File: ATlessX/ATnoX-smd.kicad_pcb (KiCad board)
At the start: 4 copper layers, 80 x 47 mm, 32 parts, among them J1 EXT_PWR_SW, J2 ATX, J3 AT, J4 PWR_LED, SW1 Power, U1 74LS74, U2 74LS14, U3 L7905

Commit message: Rev 3
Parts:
- added C5: 100nF, Capacitor_SMD:C_1206_3216Metric_Pad1.42x1.75mm_HandSolder, B.Cu at (111.8, 90.2)
- added C6: 100nF, Capacitor_SMD:C_1206_3216Metric_Pad1.42x1.75mm_HandSolder, B.Cu at (128.3, 91.4)
- added C7: 6.8pF, Capacitor_SMD:C_1206_3216Metric_Pad1.42x1.75mm_HandSolder, B.Cu at (119.4, 111.8)
- added C8: 6.8pF, Capacitor_SMD:C_1206_3216Metric_Pad1.42x1.75mm_HandSolder, B.Cu at (125.7, 111.8)
- added R10: 100K, Resistor_SMD:R_1206_3216Metric_Pad1.42x1.75mm_HandSolder, B.Cu at (111.8, 109.2)
- added R11: 10M, Resistor_SMD:R_1206_3216Metric_Pad1.42x1.75mm_HandSolder, B.Cu at (106.7, 101.6)
- added U4: 74HCT4060, Package_SO:SOIC-16_3.9x9.9mm_P1.27mm, B.Cu at (114.3, 99.1)
- added U5: 74HC73, Package_SO:SOIC-14_3.9x8.7mm_P1.27mm, B.Cu at (125.7, 99.1)
- added Y1: 3.2768, Crystal:Crystal_SMD_HC49-SD, B.Cu at (121.9, 108.0)
- moved C4 2.54 mm to (106.7, 95.2)
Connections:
- J2 pad 1: Net-(J2-Pad1) -> (no net)
- J2 pad 11: Net-(J2-Pad11) -> (no net)
- J2 pad 18: Net-(J2-Pad18) -> (no net)
- J2 pad 2: Net-(J2-Pad2) -> (no net)
- J3 pad 6: Net-(J3-Pad6) -> /TICK
- U1 pad 8: Net-(U1-Pad8) -> (no net)
- U1 pad 9: Net-(U1-Pad9) -> (no net)
- U2 pad 10: Net-(U2-Pad10) -> (no net)
- U2 pad 12: Net-(U2-Pad12) -> (no net)
- U2 pad 8: Net-(U2-Pad8) -> (no net)
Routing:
- net VCC: track 104.0 -> 206.7 mm, vias 1 -> 2
- net Net-(C8-Pad1): track 0.00 -> 62.5 mm
- net Net-(R10-Pad1): track 0.00 -> 18.5 mm
- net Net-(U4-Pad7): track 0.00 -> 17.9 mm, vias 0 -> 2
- net Net-(U5-Pad12): track 0.00 -> 17.7 mm, vias 0 -> 2
- net /TICK: track 0.00 -> 17.5 mm
- net Net-(C7-Pad1): track 0.00 -> 10.5 mm
- net /~PS_ON: track 68.5 -> 58.9 mm, vias 0 -> 1
- net Net-(U1-Pad4): track 28.6 -> 34.2 mm
- net Net-(C1-Pad1): track 24.0 -> 28.5 mm
- net /-12V: track 81.7 -> 85.3 mm, vias 1 -> 3
- net GND: track 412.3 -> 414.7 mm, vias 2 -> 4
- net Net-(C2-Pad1): track 22.0 -> 24.3 mm
- net /PWR_SW: track 13.6 -> 12.9 mm
- net /-5V: track 65.0 -> 65.7 mm
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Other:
- board text added: "rev. 3.0"
- board text removed: "rev. 2.5"

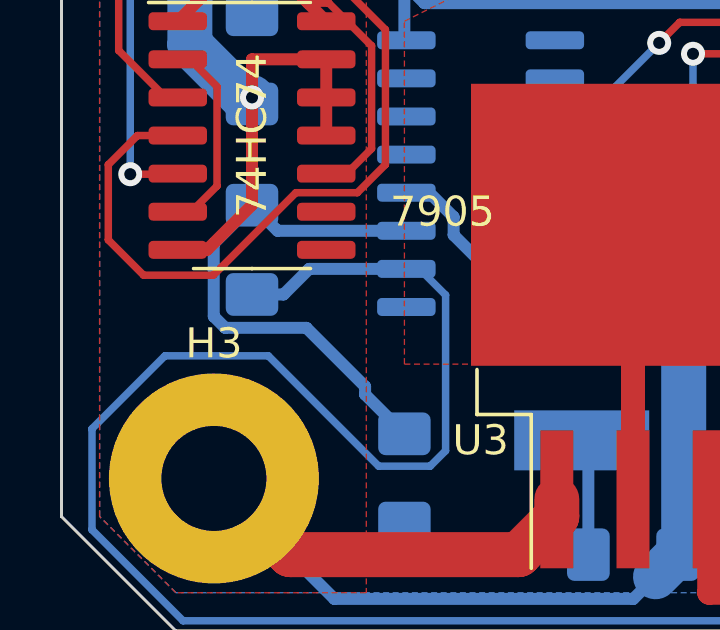
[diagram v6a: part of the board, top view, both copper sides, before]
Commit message: Clear a DRC issue
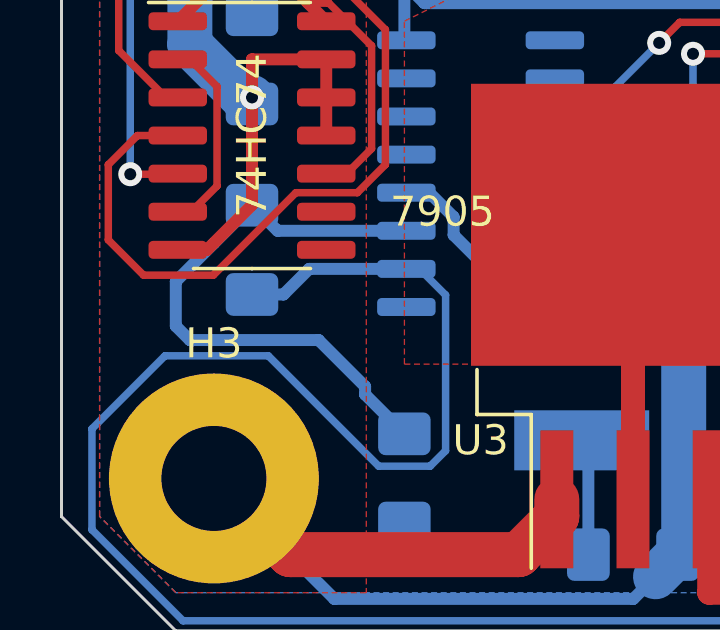
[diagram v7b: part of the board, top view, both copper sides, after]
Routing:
- net Net-(R10-Pad1): track 18.5 -> 20.4 mm
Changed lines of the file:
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@@
     (thickness 1.6)
     (drawings 28)
-    (tracks 425)
+    (tracks 426)
     (zones 0)
     (modules 41)
@@
   (page A4)
   (layers
-    (0 F.Cu signal hide)
-    (1 In1.Cu power hide)
-    (2 In2.Cu power hide)
-    (31 B.Cu signal hide)
+    (0 F.Cu signal)
+    (1 In1.Cu power)
+    (2 In2.Cu power)
+    (31 B.Cu signal)
     (32 B.Adhes user)
     (33 F.Adhes user)
@@
   (segment (start 111.76 107.732) (end 110.45 106.422) (width 0.4) (layer B.Cu) (net 24))
   (segment (start 110.45 106.422) (end 110.45 106.156) (width 0.4) (layer B.Cu) (net 24))
-  (segment (start 110.45 106.156) (end 108.494 104.2) (width 0.4) (layer B.Cu) (net 24))
-  (segment (start 108.494 104.2) (end 105.786 104.2) (width 0.4) (layer B.Cu) (net 24))
-  (segment (start 105.786 104.2) (end 105.405 103.819) (width 0.4) (layer B.Cu) (net 24))
-  (segment (start 105.405 103.819) (end 105.405 101.388) (width 0.4) (layer B.Cu) (net 24))
   (segment (start 105.405 101.388) (end 106.68 100.112) (width 0.4) (layer B.Cu) (net 24))
   (segment (start 106.68 100.112) (end 107.106 100.5385) (width 0.4) (layer B.Cu) (net 24))
   (segment (start 107.106 100.5385) (end 106.68 100.1125) (width 0.25) (layer B.Cu) (net 24))
+  (segment (start 108.90129 104.60729) (end 104.60729 104.60729) (width 0.4) (layer B.Cu) (net 24))
+  (segment (start 110.45 106.156) (end 108.90129 104.60729) (width 0.4) (layer B.Cu) (net 24))
+  (segment (start 104.60729 104.60729) (end 104.14 104.14) (width 0.4) (layer B.Cu) (net 24))
+  (segment (start 104.14 102.653) (end 105.405 101.388) (width 0.4) (layer B.Cu) (net 24))
+  (segment (start 104.14 104.14) (end 104.14 102.653) (width 0.4) (layer B.Cu) (net 24))
   (segment (start 137.75 104.14) (end 136.0747 104.14) (width 0.25) (layer B.Cu) (net 25))
   (segment (start 123.255 101.6) (end 123.6925 101.6) (width 0.25) (layer B.Cu) (net 25))

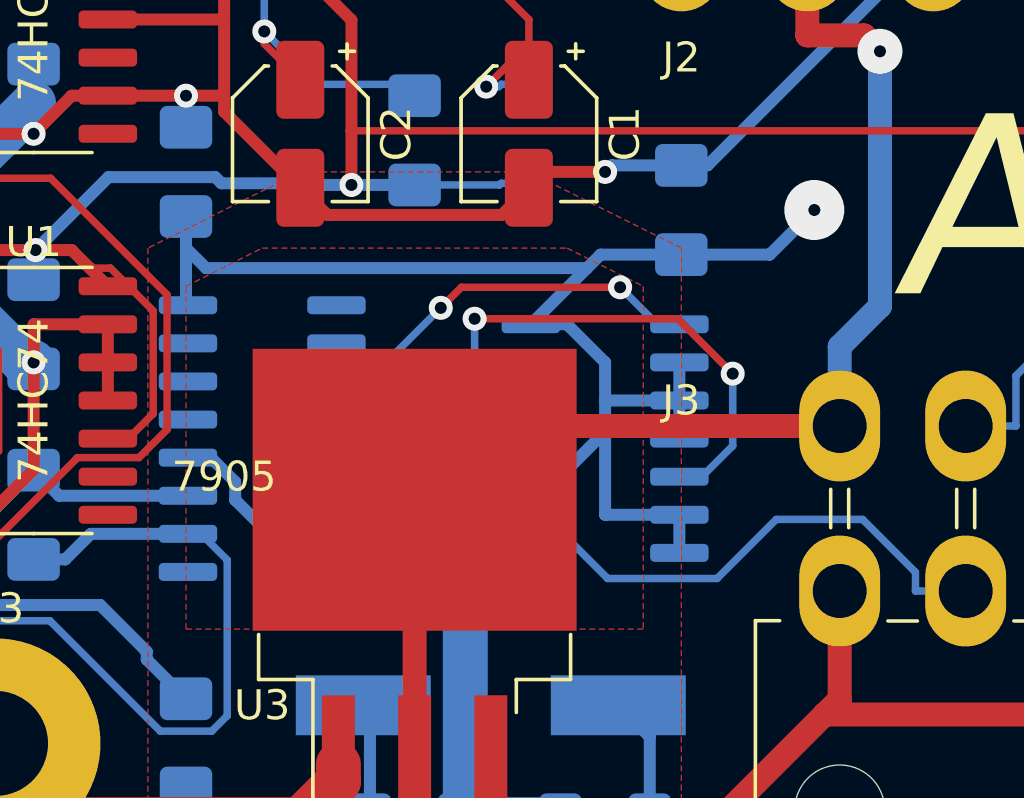
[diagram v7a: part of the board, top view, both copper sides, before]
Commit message: Remove tracks ending in a no routing zone
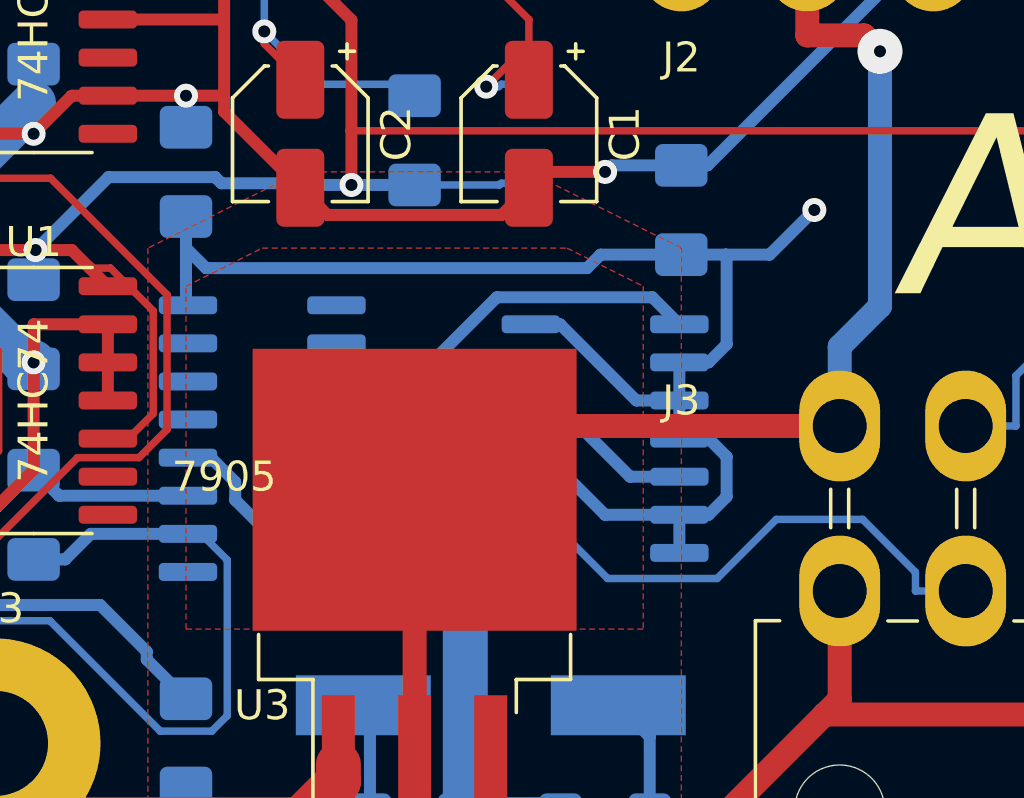
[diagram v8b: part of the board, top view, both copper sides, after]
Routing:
- net Net-(U5-Pad12): track 17.7 -> 7.19 mm, vias 2 -> 0
- net VCC: track 206.7 -> 210.2 mm
- net GND: track 414.7 -> 415.5 mm
- net Net-(U4-Pad7): track 17.9 -> 18.2 mm, vias 2 -> 0
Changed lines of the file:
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@@
     (thickness 1.6)
     (drawings 28)
-    (tracks 426)
+    (tracks 428)
     (zones 0)
     (modules 41)
@@
     (33 F.Adhes user)
     (34 B.Paste user)
-    (35 F.Paste user)
+    (35 F.Paste user hide)
     (36 B.SilkS user)
     (37 F.SilkS user)
     (38 B.Mask user)
-    (39 F.Mask user)
+    (39 F.Mask user hide)
     (40 Dwgs.User user)
     (41 Cmts.User user)
@@
   (segment (start 121.0704 111.76) (end 124.242 111.76) (width 1.5) (layer B.Cu) (net 1))
   (segment (start 120.868 111.76) (end 121.0704 111.76) (width 1.5) (layer B.Cu) (net 1))
-  (segment (start 119.0178 102.2372) (end 121.0704 104.2898) (width 1.5) (layer B.Cu) (net 1))
   (segment (start 121.0704 104.2898) (end 121.0704 111.76) (width 1.5) (layer B.Cu) (net 1))
-  (segment (start 119.0178 102.2372) (end 120.65 100.605) (width 0.4) (layer B.Cu) (net 1))
   (segment (start 120.65 100.605) (end 120.65 99.06) (width 0.4) (layer B.Cu) (net 1))
   (segment (start 120.65 99.06) (end 123.255 99.06) (width 0.4) (layer B.Cu) (net 1))
   (segment (start 116.775 103.505) (end 117.75 103.505) (width 0.4) (layer B.Cu) (net 1))
-  (segment (start 117.75 103.505) (end 119.0178 102.2372) (width 0.4) (layer B.Cu) (net 1))
   (segment (start 106.68 96.7375) (end 106.68 96.52) (width 0.4) (layer B.Cu) (net 1))
   (segment (start 106.68 87.8786) (end 104.6084 89.9502) (width 1.5) (layer B.Cu) (net 1))
@@
   (via (at 111.76 87.63) (size 0.8) (layers F.Cu B.Cu) (net 1))
   (via (at 106.68 88.9) (size 0.8) (layers F.Cu B.Cu) (net 1))
+  (segment (start 120.2856 103.505) (end 121.0704 104.2898) (width 0.4) (layer B.Cu) (net 1))
+  (segment (start 116.775 103.505) (end 120.2856 103.505) (width 0.4) (layer B.Cu) (net 1))
+  (segment (start 120.2856 103.505) (end 120.2856 100.6944) (width 0.4) (layer B.Cu) (net 1))
+  (segment (start 120.375 100.605) (end 120.65 100.605) (width 0.4) (layer B.Cu) (net 1))
+  (segment (start 120.2856 100.6944) (end 120.375 100.605) (width 0.4) (layer B.Cu) (net 1))
   (segment (start 123.19 87.25) (end 122.2647 87.25) (width 0.25) (layer B.Cu) (net 2))
   (segment (start 123.19 86.095) (end 123.0012 86.095) (width 0.25) (layer F.Cu) (net 2))
@@
   (segment (start 128.205 97.79) (end 128.205 99.06) (width 0.4) (layer B.Cu) (net 6))
   (segment (start 128.205 96.52) (end 128.205 97.79) (width 0.4) (layer B.Cu) (net 6))
-  (segment (start 125.73 97.79) (end 128.205 97.79) (width 0.4) (layer B.Cu) (net 6))
-  (segment (start 125.73 98.83) (end 125.73 97.79) (width 0.4) (layer B.Cu) (net 6))
-  (segment (start 125.128 93.3775) (end 123.255 95.25) (width 0.4) (layer B.Cu) (net 6))
-  (segment (start 128.27 92.9275) (end 125.578 92.9275) (width 0.4) (layer B.Cu) (net 6))
-  (segment (start 125.578 92.9275) (end 125.128 93.3775) (width 0.4) (layer B.Cu) (net 6))
   (segment (start 150.35 98.64) (end 154.55 98.64) (width 1.5) (layer B.Cu) (net 6))
   (segment (start 173.86 90.17) (end 172.72 90.17) (width 0.4) (layer F.Cu) (net 6))
@@
   (segment (start 172.72 82.7675) (end 171.668 82.7675) (width 0.4) (layer B.Cu) (net 6))
   (segment (start 171.668 82.7675) (end 171.45 82.55) (width 0.4) (layer B.Cu) (net 6))
-  (segment (start 128.27 92.9275) (end 131.217 92.9275) (width 0.4) (layer B.Cu) (net 6))
   (segment (start 131.217 92.9275) (end 132.704 91.44) (width 0.4) (layer B.Cu) (net 6))
   (segment (start 111.76 91.6575) (end 111.76 92.71) (width 0.4) (layer B.Cu) (net 6))
   (segment (start 111.76 92.71) (end 111.76 94.55) (width 0.4) (layer B.Cu) (net 6))
   (segment (start 111.76 94.55) (end 111.825 94.615) (width 0.4) (layer B.Cu) (net 6))
-  (segment (start 125.128 93.3775) (end 112.428 93.3775) (width 0.4) (layer B.Cu) (net 6))
-  (segment (start 112.428 93.3775) (end 111.76 92.71) (width 0.4) (layer B.Cu) (net 6))
   (segment (start 128.205 101.6) (end 128.205 102.87) (width 0.4) (layer B.Cu) (net 6))
-  (segment (start 125.73 98.83) (end 125.73 101.6) (width 0.4) (layer B.Cu) (net 6))
   (segment (start 125.73 101.6) (end 128.205 101.6) (width 0.4) (layer B.Cu) (net 6))
-  (segment (start 123.255 95.25) (end 124.46 95.25) (width 0.4) (layer B.Cu) (net 6))
-  (segment (start 124.46 95.25) (end 125.73 96.52) (width 0.4) (layer B.Cu) (net 6))
-  (segment (start 125.73 96.52) (end 125.73 97.79) (width 0.4) (layer B.Cu) (net 6))
   (segment (start 123.255 100.33) (end 124.23 100.33) (width 0.4) (layer B.Cu) (net 6))
-  (segment (start 124.23 100.33) (end 125.73 98.83) (width 0.4) (layer B.Cu) (net 6))
   (segment (start 154.55 98.64) (end 154.55 94.37) (width 1.5) (layer In1.Cu) (net 6))
   (segment (start 154.55 94.37) (end 157.48 91.44) (width 1.5) (layer In1.Cu) (net 6))
@@
   (segment (start 143.87 74.47) (end 140.87 77.47) (width 1.5) (layer In1.Cu) (net 6))
   (via (at 171.45 82.55) (size 0.8) (layers F.Cu B.Cu) (net 6))
-  (via (at 132.704 91.44) (size 2) (layers F.Cu B.Cu) (net 6))
+  (via (at 132.704 91.44) (size 0.8) (drill 0.4) (layers F.Cu B.Cu) (net 6) (status 1000000))
+  (segment (start 124.46 100.33) (end 125.73 101.6) (width 0.4) (layer B.Cu) (net 6))
+  (segment (start 123.255 100.33) (end 124.46 100.33) (width 0.4) (layer B.Cu) (net 6))
+  (segment (start 126.77 97.79) (end 128.205 97.79) (width 0.4) (layer B.Cu) (net 6))
+  (segment (start 124.23 95.25) (end 126.77 97.79) (width 0.4) (layer B.Cu) (net 6))
+  (segment (start 123.255 95.25) (end 124.23 95.25) (width 0.4) (layer B.Cu) (net 6))
+  (segment (start 129.78001 100.99999) (end 129.18 101.6) (width 0.4) (layer B.Cu) (net 6))
+  (segment (start 129.78001 99.66001) (end 129.78001 100.99999) (width 0.4) (layer B.Cu) (net 6))
+  (segment (start 129.18 99.06) (end 129.78001 99.66001) (width 0.4) (layer B.Cu) (net 6))
+  (segment (start 129.18 101.6) (end 128.205 101.6) (width 0.4) (layer B.Cu) (net 6))
+  (segment (start 128.205 99.06) (end 129.18 99.06) (width 0.4) (layer B.Cu) (net 6))
+  (segment (start 129.78001 95.91999) (end 129.78001 92.95001) (width 0.4) (layer B.Cu) (net 6))
+  (segment (start 129.18 96.52) (end 129.78001 95.91999) (width 0.4) (layer B.Cu) (net 6))
+  (segment (start 128.205 96.52) (end 129.18 96.52) (width 0.4) (layer B.Cu) (net 6))
+  (segment (start 129.78001 92.95001) (end 129.7575 92.9275) (width 0.4) (layer B.Cu) (net 6))
+  (segment (start 129.7575 92.9275) (end 131.217 92.9275) (width 0.4) (layer B.Cu) (net 6))
+  (segment (start 128.27 92.9275) (end 129.7575 92.9275) (width 0.4) (layer B.Cu) (net 6))
+  (segment (start 125.578 92.9275) (end 128.27 92.9275) (width 0.4) (layer B.Cu) (net 6))
+  (segment (start 125.128 93.3775) (end 125.578 92.9275) (width 0.4) (layer B.Cu) (net 6))
+  (segment (start 112.428 93.3775) (end 125.128 93.3775) (width 0.4) (layer B.Cu) (net 6))
+  (segment (start 111.76 92.71) (end 112.428 93.3775) (width 0.4) (layer B.Cu) (net 6))
   (segment (start 176.66 90.17) (end 177.8551 91.3651) (width 0.25) (layer F.Cu) (net 7))
   (segment (start 176.7475 90.17) (end 176.7475 90.2575) (width 0.25) (layer B.Cu) (net 7))
@@
   (segment (start 134.3161 101.7532) (end 136.0747 103.5118) (width 0.25) (layer B.Cu) (net 25))
   (segment (start 136.0747 103.5118) (end 136.0747 104.14) (width 0.25) (layer B.Cu) (net 25))
-  (segment (start 126.2304 94.0161) (end 127.4643 95.25) (width 0.25) (layer B.Cu) (net 26))
   (segment (start 127.4643 95.25) (end 128.205 95.25) (width 0.25) (layer B.Cu) (net 26))
-  (segment (start 120.253 94.7011) (end 120.938 94.0161) (width 0.25) (layer F.Cu) (net 26))
-  (segment (start 120.938 94.0161) (end 126.2304 94.0161) (width 0.25) (layer F.Cu) (net 26))
   (segment (start 116.775 102.235) (end 117.1523 102.235) (width 0.25) (layer B.Cu) (net 26))
-  (segment (start 117.1523 102.235) (end 118.1069 101.2804) (width 0.25) (layer B.Cu) (net 26))
-  (segment (start 118.1069 101.2804) (end 118.1069 96.8472) (width 0.25) (layer B.Cu) (net 26))
-  (segment (start 118.1069 96.8472) (end 120.253 94.7011) (width 0.25) (layer B.Cu) (net 26))
-  (via (at 126.2304 94.0161) (size 0.8) (layers F.Cu B.Cu) (net 26))
-  (via (at 120.253 94.7011) (size 0.8) (layers F.Cu B.Cu) (net 26))
-  (segment (start 121.3799 95.0648) (end 121.3799 96.3548) (width 0.25) (layer B.Cu) (net 27))
-  (segment (start 121.3799 96.3548) (end 122.8151 97.79) (width 0.25) (layer B.Cu) (net 27))
+  (segment (start 127.30499 94.34999) (end 128.205 95.25) (width 0.4) (layer B.Cu) (net 26))
+  (segment (start 122.119334 94.34999) (end 127.30499 94.34999) (width 0.4) (layer B.Cu) (net 26))
+  (segment (start 118.745 101.24) (end 118.745 97.724324) (width 0.4) (layer B.Cu) (net 26))
+  (segment (start 117.75 102.235) (end 118.745 101.24) (width 0.4) (layer B.Cu) (net 26))
+  (segment (start 118.745 97.724324) (end 122.119334 94.34999) (width 0.4) (layer B.Cu) (net 26))
+  (segment (start 116.775 102.235) (end 117.75 102.235) (width 0.4) (layer B.Cu) (net 26))
   (segment (start 122.8151 97.79) (end 123.255 97.79) (width 0.25) (layer B.Cu) (net 27))
-  (segment (start 129.9837 96.8953) (end 128.1532 95.0648) (width 0.25) (layer F.Cu) (net 27))
-  (segment (start 128.1532 95.0648) (end 121.3799 95.0648) (width 0.25) (layer F.Cu) (net 27))
   (segment (start 128.205 100.33) (end 128.9555 100.33) (width 0.25) (layer B.Cu) (net 27))
-  (segment (start 128.9555 100.33) (end 129.9837 99.3018) (width 0.25) (layer B.Cu) (net 27))
-  (segment (start 129.9837 99.3018) (end 129.9837 96.8953) (width 0.25) (layer B.Cu) (net 27))
-  (via (at 121.3799 95.0648) (size 0.8) (layers F.Cu B.Cu) (net 27))
-  (via (at 129.9837 96.8953) (size 0.8) (layers F.Cu B.Cu) (net 27))
+  (segment (start 124.020676 97.79) (end 123.255 97.79) (width 0.4) (layer B.Cu) (net 27))
+  (segment (start 126.560676 100.33) (end 124.020676 97.79) (width 0.4) (layer B.Cu) (net 27))
+  (segment (start 128.205 100.33) (end 126.560676 100.33) (width 0.4) (layer B.Cu) (net 27))
   (zone (net 10) (net_name /-12V) (layer F.Cu) (hatch edge 0.508)
     (connect_pads yes (clearance 0.508))
